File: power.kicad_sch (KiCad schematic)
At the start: 19 parts, among them U2 LM66100DCKT, U3 LM66100DCKT, U4 LM2735XSD_NOPB, U5 TPS63031DSK

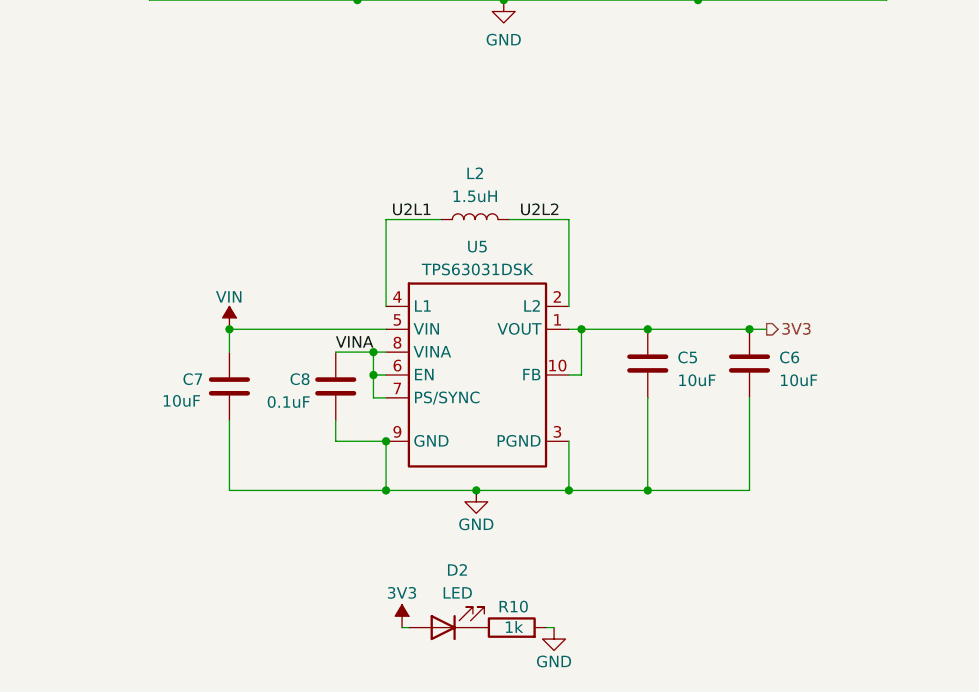
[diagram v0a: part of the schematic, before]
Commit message: schematic rough draft except fpc
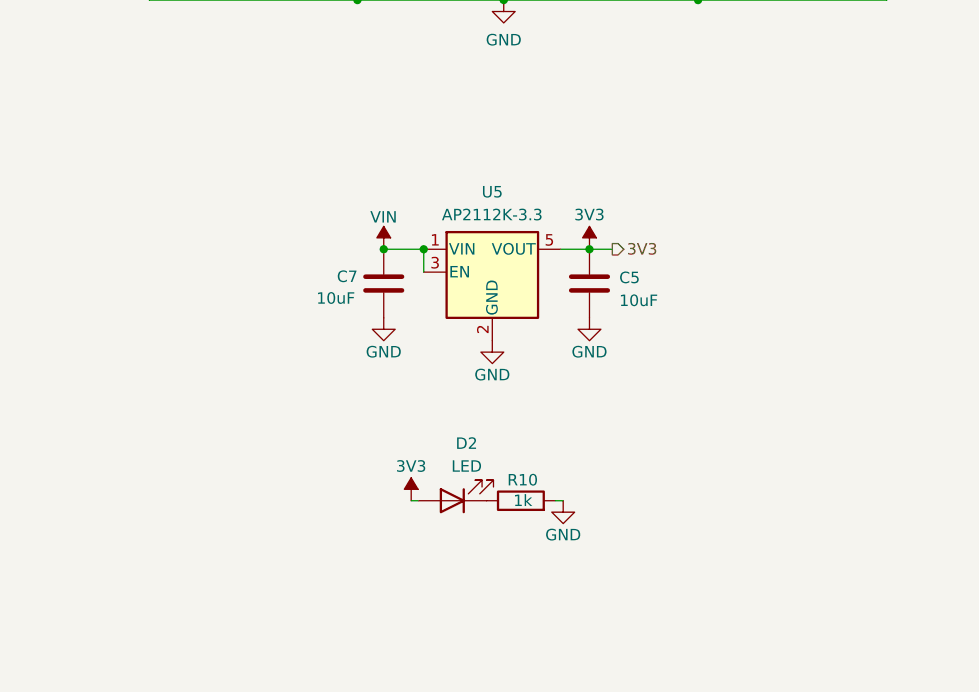
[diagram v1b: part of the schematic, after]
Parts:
- removed C6: 10uF, Capacitor_SMD:C_0603_1608Metric, symbol Device:C
- removed C8: 0.1uF, Capacitor_SMD:C_0402_1005Metric, symbol Device:C
- removed L2: 1.5uH, v12e:IND_Murata_LQH3NPN1R5MJRL, symbol Device:L
- removed U5: TPS63031DSK, Package_SON:WSON-10-1EP_2.5x2.5mm_P0.5mm_EP1.2x2mm, symbol Regulator_Switching:TPS63031DSK
- added U5: AP2112K-3.3, Package_TO_SOT_SMD:SOT-23-5, symbol Regulator_Linear:AP2112K-3.3
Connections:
- net 3V3: now also U5.5 (VOUT)
- net EPAD: now also U5.2 (GND)
- net VIN: now also U5.1 (VIN), U5.3 (EN)
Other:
- moved on the sheet: C5, C7, D2, R10

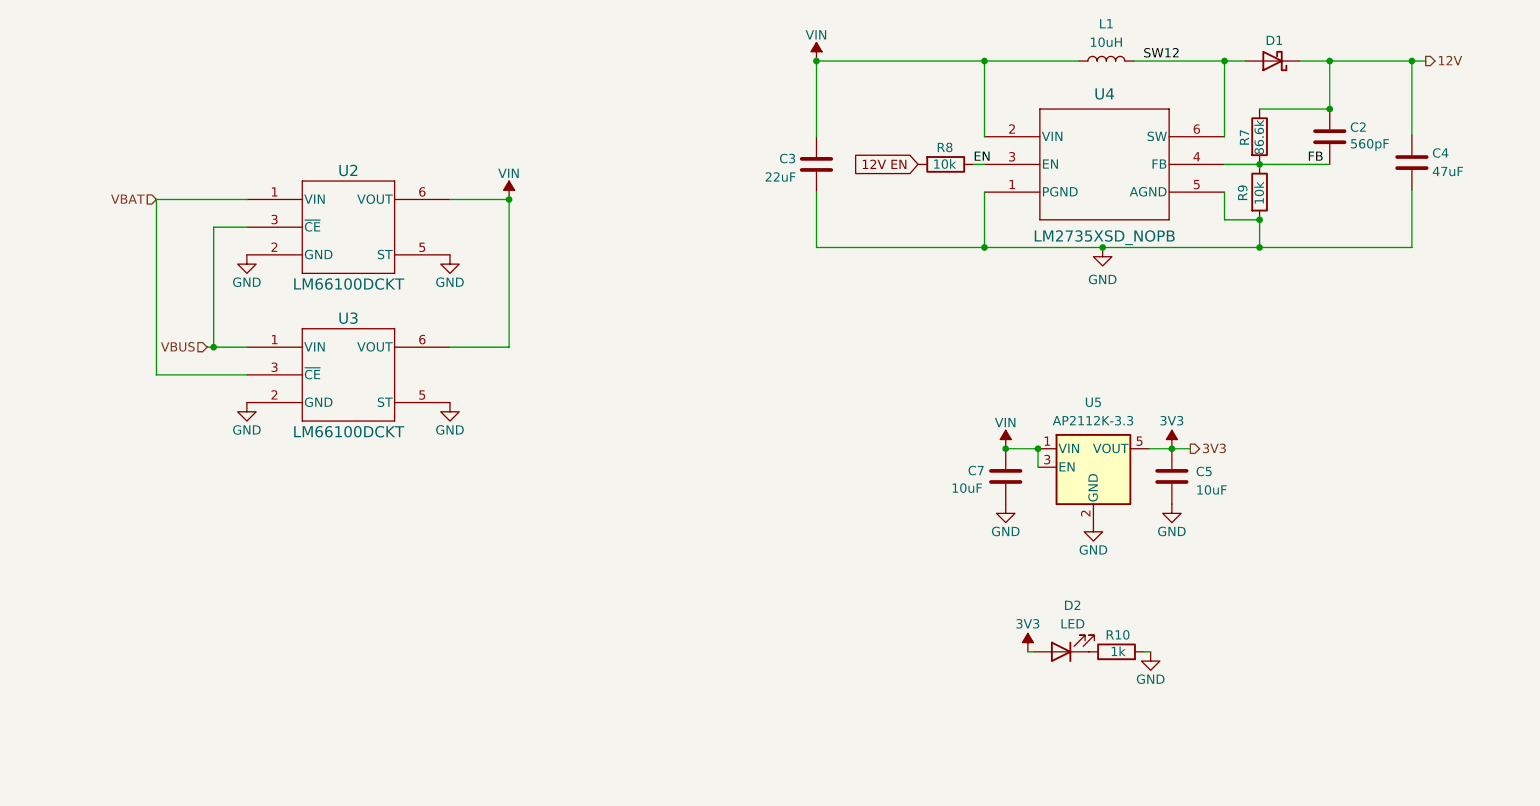
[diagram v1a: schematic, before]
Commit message: schematic draft 2; no FPC connections, no testpoints
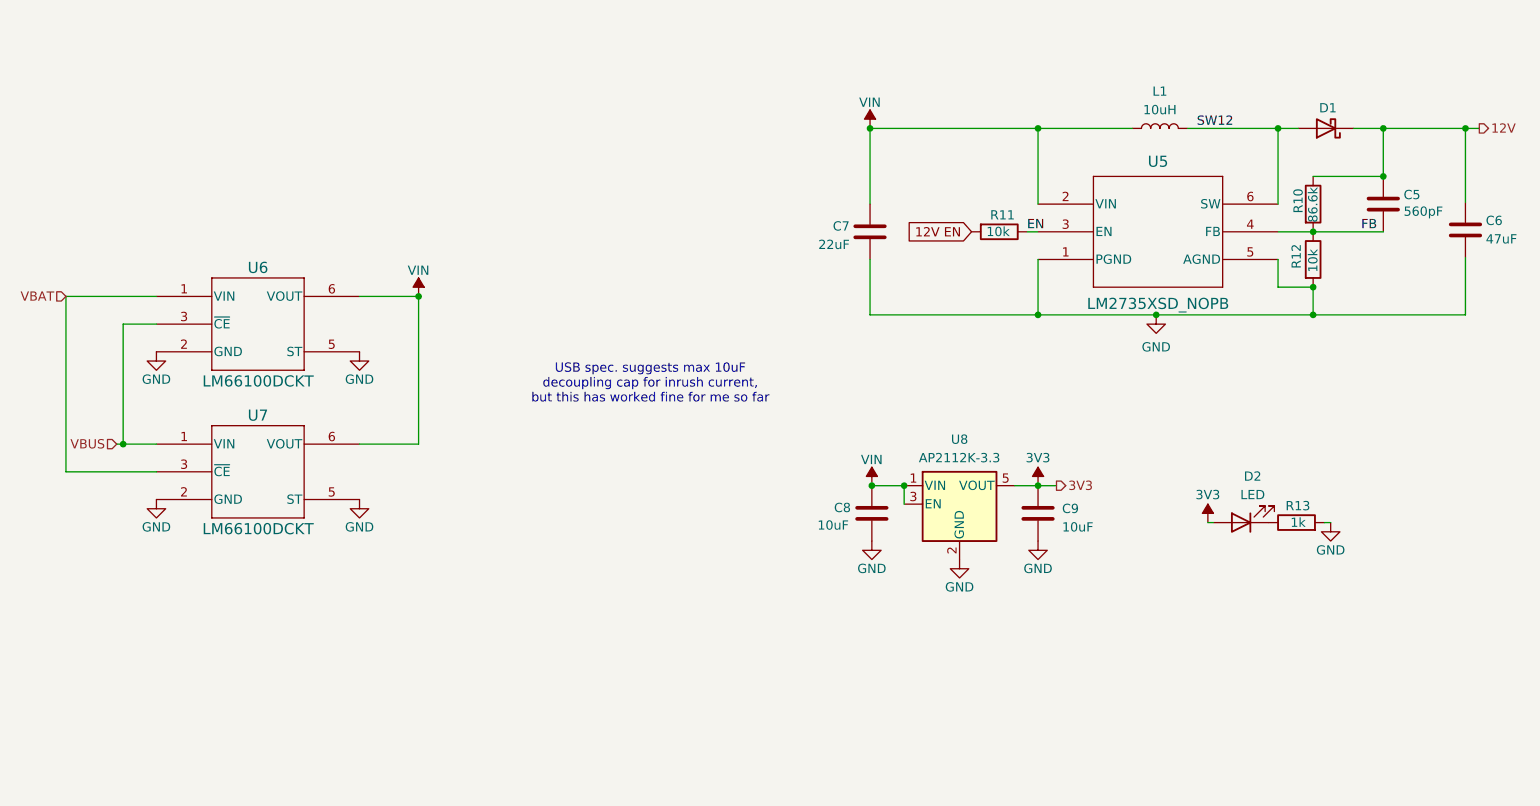
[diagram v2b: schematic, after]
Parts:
- D2: footprint v12e:LED_0603_RA_TJ-S1706CL6T5ALC9Y-A5 -> nrf52-controller:LED_0603_RA_TJ-S1706CL6T5ALC9Y-A5
- L1: footprint v12e:IND_357100_WRE -> nrf52-controller:IND_357100_WRE
- U6: renamed from U2; footprint v12e:SC70_DCK6_TI -> nrf52-controller:SC70_DCK6_TI
- U7: renamed from U3; footprint v12e:SC70_DCK6_TI -> nrf52-controller:SC70_DCK6_TI
- renumbered C2 to C5, C4 to C6, C3 to C7, C7 to C8, C5 to C9, R7 to R10, R8 to R11, R9 to R12, R10 to R13, U4 to U5, U5 to U8
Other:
- note added: "USB spec. suggests max 10uF decoupling cap for inrush current, but this has worked fine for me so far"
- moved on the sheet: C5, C6, C7, C8, C9, D1, D2, L1, R10, R11, R12, R13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

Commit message: layout start
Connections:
- net 12V EN renamed 12V_EN2
- net 12V_EN2: now also U5.3 (EN)
- net EN renamed 12V_EN1
- net 12V_EN1: no longer U5.3 (EN)
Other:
- moved on the sheet: R11
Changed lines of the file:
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@@
 	(wire
 		(pts
-			(xy 181.356 78.105) (xy 182.88 78.105)
+			(xy 172.085 78.105) (xy 182.88 78.105)
 		)
 		(stroke
@@
 		)
 	)
-	(label "EN"
-		(at 181.356 78.105 0)
+	(label "12V_EN2"
+		(at 173.99 78.105 0)
 		(fields_autoplaced yes)
 		(effects
@@
 			)
 			(justify left bottom)
-		)
-	)
-	(global_label "12V EN"
-		(shape input)
-		(at 173.736 78.105 180)
-		(fields_autoplaced yes)
-		(effects
-			(font
-				(size 1.27 1.27)
-			)
-			(justify right)
-		)
-		(property "Intersheetrefs" "${INTERSHEET_REFS}"
-			(at 163.8755 78.105 0)
-			(effects
-				(font
-					(size 1.27 1.27)
-				)
-				(justify right)
-				(hide yes)
-			)
 		)
 	)
@@
 		)
 	)
+	(hierarchical_label "12V_EN1"
+		(shape input)
+		(at 172.085 70.485 180)
+		(fields_autoplaced yes)
+		(effects
+			(font
+				(size 1.27 1.27)
+			)
+			(justify right)
+		)
+	)
 	(hierarchical_label "VBAT"
 		(shape input)
@@
 		(dnp no)
 		(property "Reference" "R12"
-			(at 218.44 83.185 90)
+			(at 222.25 81.915 0)
 			(effects
 				(font
@@
 	(symbol
 		(lib_id "Device:R")
-		(at 177.546 78.105 270)
+		(at 172.085 74.295 0)
 		(unit 1)
 		(exclude_from_sim no)
@@
 		(dnp no)
 		(property "Reference" "R11"
-			(at 176.276 75.819 90)
+			(at 167.005 74.295 0)
 			(effects
 				(font
@@
 		)
 		(property "Value" "10k"
-			(at 175.768 78.105 90)
+			(at 172.085 76.073 90)
 			(effects
 				(font
@@
 		)
 		(property "Footprint" "Resistor_SMD:R_0402_1005Metric"
-			(at 177.546 76.327 90)
+			(at 170.307 74.295 90)
 			(effects
 				(font
@@
 		)
 		(property "Datasheet" "~"
-			(at 177.546 78.105 0)
-			(effects
-				(font
-					(size 1.27 1.27)
-				)
-				(hide yes)
-			)
-		)
-		(property "Description" ""
-			(at 177.546 78.105 0)
+			(at 172.085 74.295 0)
+			(effects
+				(font
+					(size 1.27 1.27)
+				)
+				(hide yes)
+			)
+		)
+		(property "Description" ""
+			(at 172.085 74.295 0)
 			(effects
 				(font
@@
 		)
 		(property "JLCPCB Part #" "C25744"
-			(at 177.546 78.105 90)
+			(at 172.085 74.295 90)
 			(effects
 				(font
@@
 		(dnp no)
 		(property "Reference" "R10"
-			(at 218.694 75.565 90)
-			(effects
-				(font
+			(at 222.25 74.295 0)
+			(effects
+				(font
